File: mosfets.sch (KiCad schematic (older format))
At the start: 45 parts, among them Q1 ZXTC2045E6, Q10 ZXTC2045E6, Q11 IRFP4668PBF, Q12 IRFP4668PBF, Q2 ZXTC2045E6, Q3 IRFP4668PBF, Q4 IRFP4668PBF, Q5 ZXTC2045E6, Q6 ZXTC2045E6, Q7 IRFP4668PBF, Q8 IRFP4668PBF, Q9 ZXTC2045E6

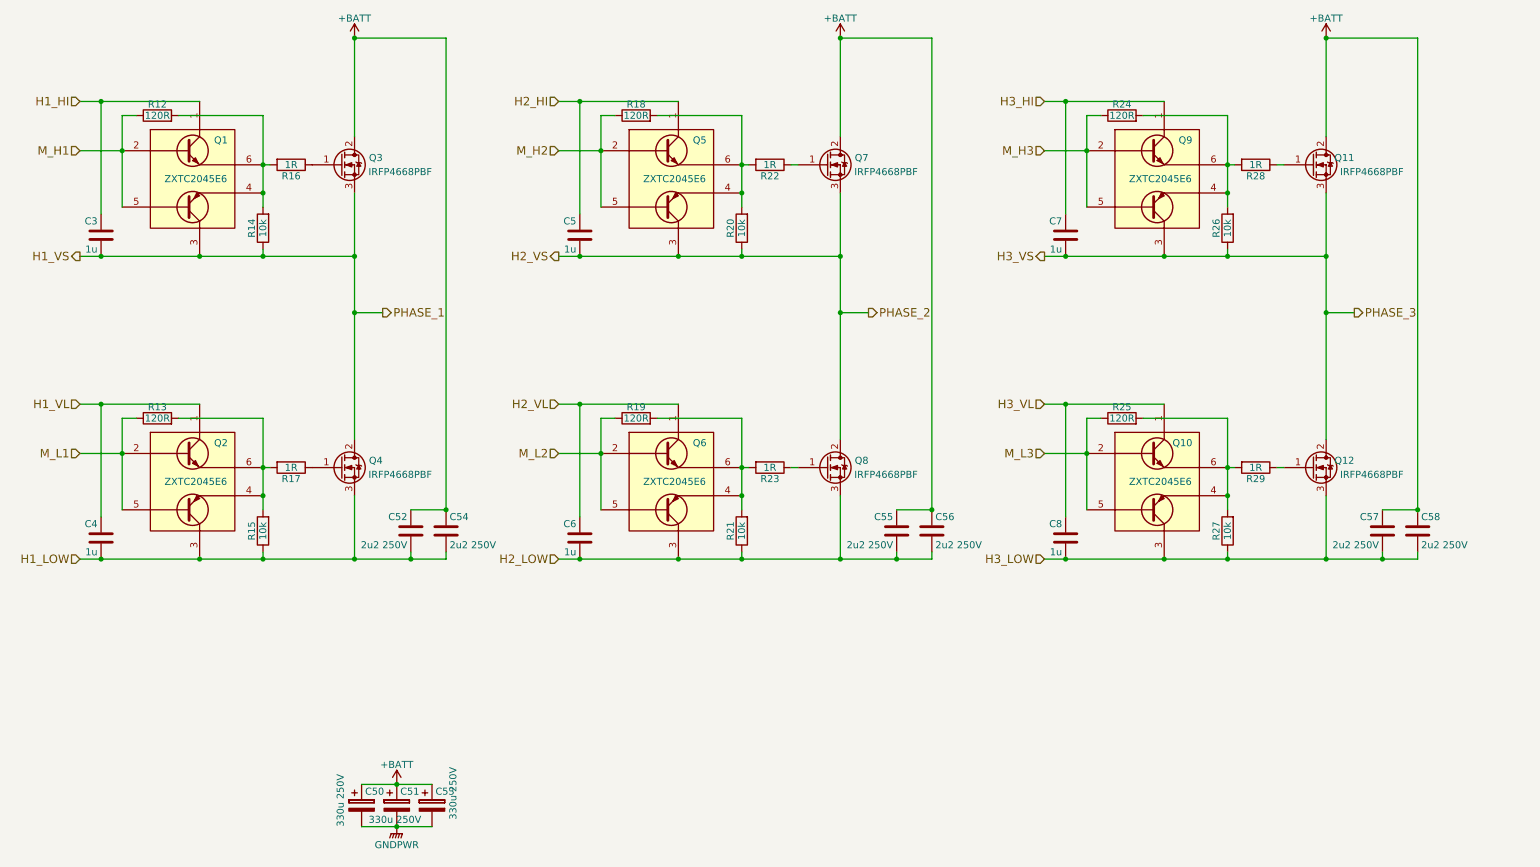
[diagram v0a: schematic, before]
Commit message: - removed 1 MOSFET of each group (no space) - removed 2 DC buffer caps (no space) - power stage routed - shunts and amps routed - post driver routed - pre driver HV routed
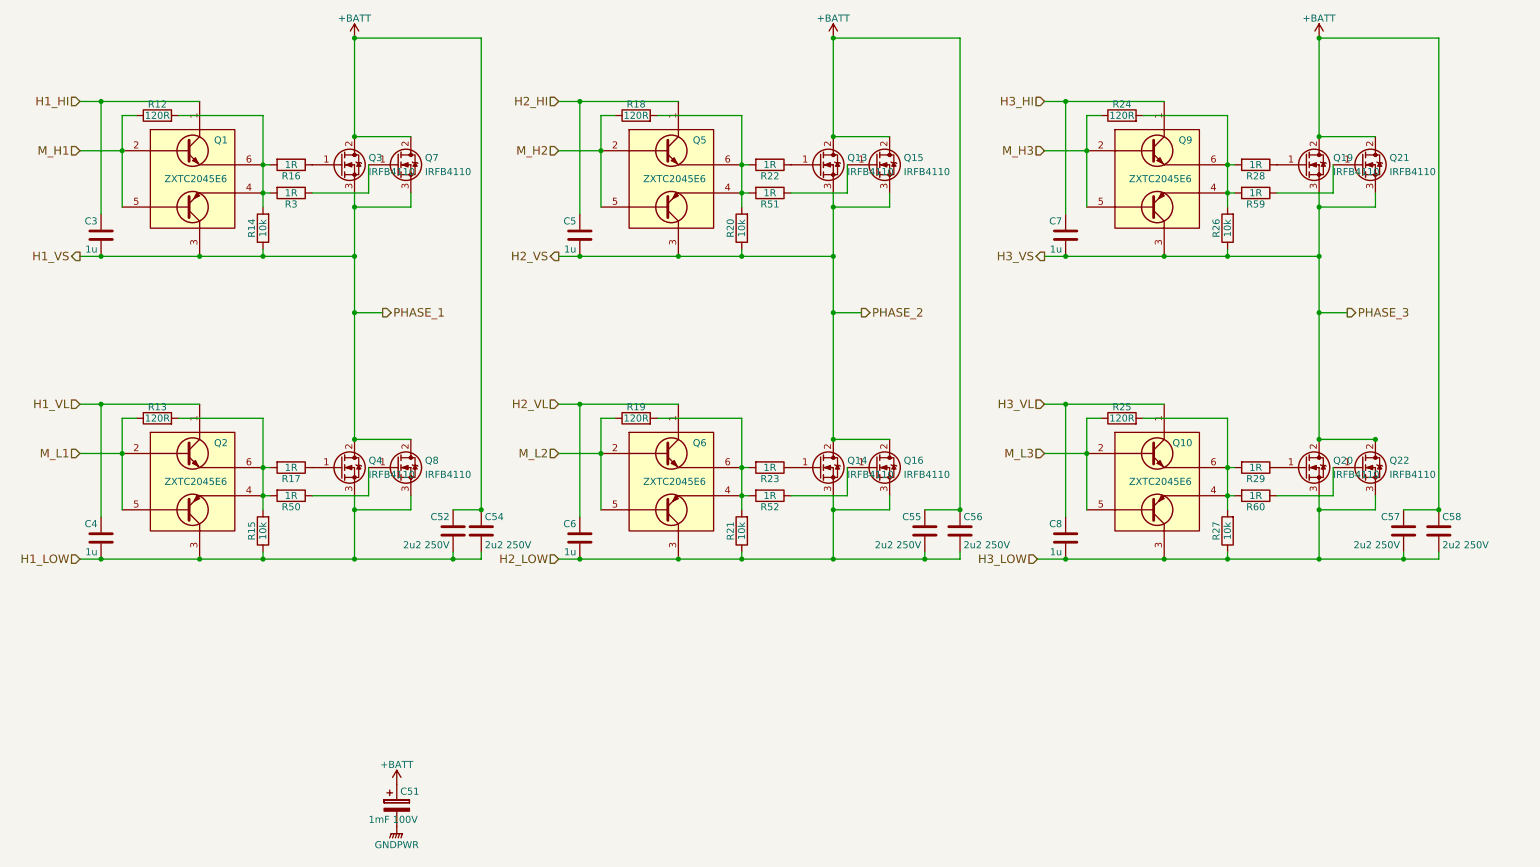
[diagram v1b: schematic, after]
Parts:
- removed C50, C53: 330u 250V, alexmod:C_Radial_D22_P10, symbol CP
- removed Q11, Q12: IRFP4668PBF, alexmod:TO-264_flat_reverse, symbol Q_NMOS_GDS
- added Q13, Q14, Q15, Q16, Q19, Q20, Q21, Q22: IRFB4110, alexmod:TO220GDS_notab_rev, symbol Q_NMOS_GDS
- added R3, R50, R51, R52, R59, R60: 1R, Resistors_SMD:R_0805, symbol R
- C51: value 330u 250V -> 1mF 100V
- Q3, Q4, Q7, Q8: value IRFP4668PBF -> IRFB4110; footprint alexmod:TO-264_flat_reverse -> alexmod:TO220GDS_notab_rev
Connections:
- net +BATT: now also Q13.2 (D), Q15.2 (D), Q19.2 (D), Q21.2 (D)
- net H1_LOW: now also Q8.3 (S)
- net H1_VS: now also Q7.3 (S), Q8.2 (D)
- net H2_LOW: now also Q14.3 (S), Q16.3 (S); no longer Q8.3 (S)
- net H2_VS: now also Q13.3 (S), Q14.2 (D), Q15.3 (S), Q16.2 (D); no longer Q7.3 (S), Q8.2 (D)
- net H3_LOW: now also Q20.3 (S), Q22.3 (S)
- net H3_VS: now also Q19.3 (S), Q20.2 (D), Q21.3 (S), Q22.2 (D)
- net at R29.1: now also Q20.1 (G)
- net at Q10.4 (E2), Q10.6 (E1), R25.2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: now also R60.2
- net at R28.1: now also Q19.1 (G)
- net at Q9.4 (E2), Q9.6 (E1), R24.2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: now also R59.2
- net at R23.1: now also Q14.1 (G); no longer Q8.1 (G)
- net at Q6.4 (E2), Q6.6 (E1), R19.2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: now also R52.2
- net at R22.1: now also Q13.1 (G); no longer Q7.1 (G)
- net at Q5.4 (E2), Q5.6 (E1), R18.2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: now also R51.2
- net at Q2.4 (E2), Q2.6 (E1), R13.2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: now also R50.2
- net at Q1.4 (E2), Q1.6 (E1), R12.2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: now also R3.2
- new net: Q7.1 (G), R3.1
- new net: Q8.1 (G), R50.1
- new net: Q16.1 (G), R52.1
- new net: Q15.1 (G), R51.1
- new net: Q21.1 (G), R59.1
- new net: Q22.1 (G), R60.1
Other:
- moved on the sheet: C52, C54, C55, C56, C57, C58

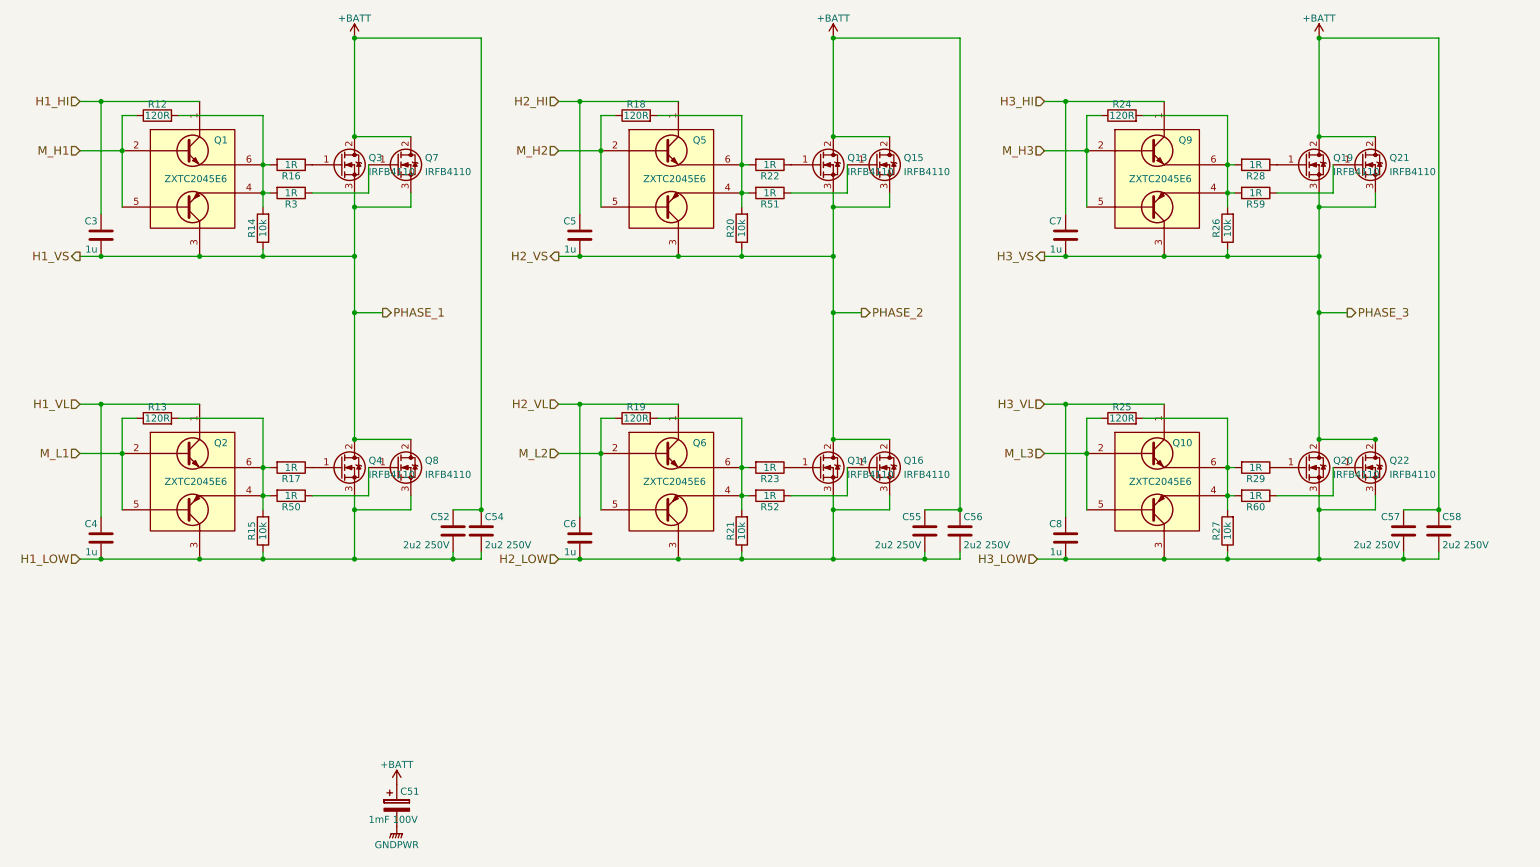
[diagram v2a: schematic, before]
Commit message: - basis commit for V1.1 - did an great overhaul of high current paths - fixed wrong 3V3 reg pin out - blew the IO connector up to 8 pins (turns out 7pin is rare) - changed shunt to 2512 - changed hf caps to double 1210 - two input caps - pin outs for all IO on silk screen - spread the references so you can actually read them - connected the Hall/Temp pull-ups to 3V3 instead of 5V - changed vias to 0.6/0.3mm - changed text to V1.1
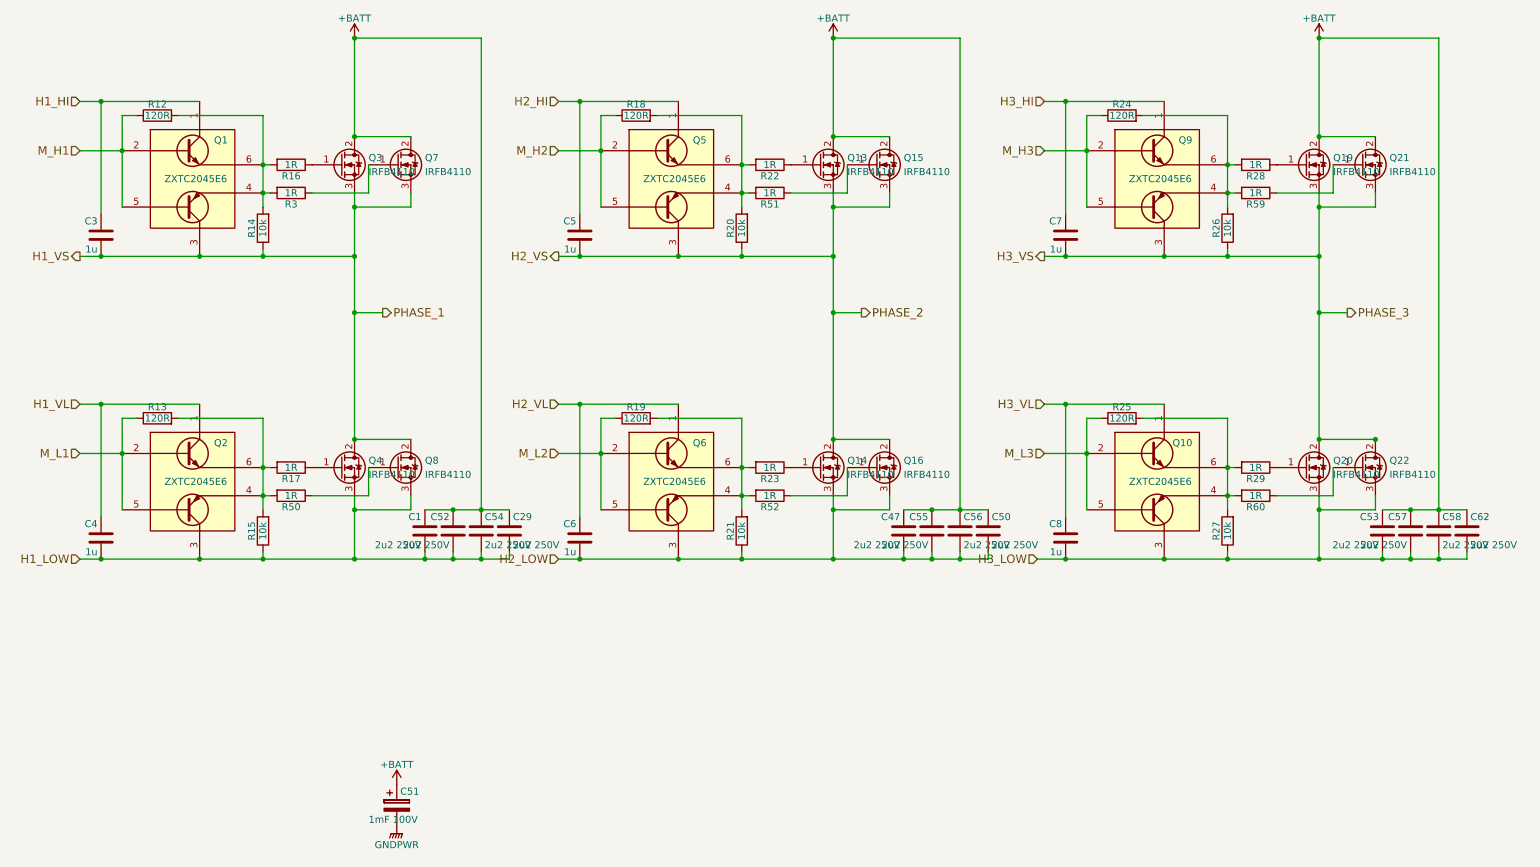
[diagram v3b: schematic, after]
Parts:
- added C1, C29, C47, C50, C53, C62: 2u2 250V, Capacitors_SMD:C_1210, symbol C
- C52, C54, C55, C56, C57, C58: footprint Capacitors_SMD:C_2220 -> Capacitors_SMD:C_1210
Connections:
- net +BATT: now also C1.1, C29.1, C47.1, C50.1, C53.1, C62.1
- net H1_LOW: now also C1.2, C29.2
- net H2_LOW: now also C47.2, C50.2
- net H3_LOW: now also C53.2, C62.2
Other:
- moved on the sheet: C55, C57
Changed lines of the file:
@@
 Connection ~ 10000 3650
 $Comp
-L +BATT #PWR025
+L +BATT #PWR026
 U 1 1 575A4EA5
 P 10000 1700
-F 0 "#PWR025" H 10000 1550 50  0001 C CNN
+F 0 "#PWR026" H 10000 1550 50  0001 C CNN
 F 1 "+BATT" H 10000 1840 50  0000 C CNN
 F 2 "" H 10000 1700 50  0000 C CNN
@@
 Connection ~ 8200 5400
 Wire Wire Line
-	8050 3250 10000 3250
+	10000 3250 8050 3250
 Wire Wire Line
 	9400 2600 9350 2600
@@
 Connection ~ 9350 4750
 Wire Wire Line
-	8000 5400 10850 5400
+	8000 5400 11050 5400
 Wire Wire Line
 	6550 3650 6750 3650
 Connection ~ 6550 3650
 $Comp
-L +BATT #PWR026
+L +BATT #PWR027
 U 1 1 589857E2
 P 6550 1700
-F 0 "#PWR026" H 6550 1550 50  0001 C CNN
+F 0 "#PWR027" H 6550 1550 50  0001 C CNN
 F 1 "+BATT" H 6550 1840 50  0000 C CNN
 F 2 "" H 6550 1700 50  0000 C CNN
@@
 Connection ~ 4750 5400
 Wire Wire Line
-	4600 3250 6550 3250
+	6550 3250 4600 3250
 Wire Wire Line
 	5950 2600 5900 2600
@@
 Connection ~ 5900 4750
 Wire Wire Line
-	4600 5400 7450 5400
+	4600 5400 7650 5400
 Wire Wire Line
 	3150 3650 3350 3650
 Connection ~ 3150 3650
 $Comp
-L +BATT #PWR027
+L +BATT #PWR028
 U 1 1 58986AF5
 P 3150 1700
-F 0 "#PWR027" H 3150 1550 50  0001 C CNN
+F 0 "#PWR028" H 3150 1550 50  0001 C CNN
 F 1 "+BATT" H 3150 1840 50  0000 C CNN
 F 2 "" H 3150 1700 50  0000 C CNN
@@
 $EndComp
 Wire Wire Line
-	1200 3250 3150 3250
+	3150 3250 1200 3250
 Wire Wire Line
 	2550 2600 2500 2600
@@
 Connection ~ 2500 4750
 Wire Wire Line
-	1200 5400 4050 5400
-$Comp
-L +BATT #PWR028
+	1200 5400 4250 5400
+$Comp
+L +BATT #PWR029
 U 1 1 58A716A6
 P 3450 7000
-F 0 "#PWR028" H 3450 6850 50  0001 C CNN
+F 0 "#PWR029" H 3450 6850 50  0001 C CNN
 F 1 "+BATT" H 3450 7140 50  0000 C CNN
 F 2 "" H 3450 7000 50  0000 C CNN
@@
 F 0 "C52" H 3875 5300 50  0000 L CNN
 F 1 "2u2 250V" H 3875 5100 50  0000 L CNN
-F 2 "Capacitors_SMD:C_2220" H 3888 5050 50  0001 C CNN
+F 2 "Capacitors_SMD:C_1210" H 3888 5050 50  0001 C CNN
 F 3 "" H 3850 5200 50  0000 C CNN
 	1    3850 5200
@@
 F 0 "C54" H 4075 5300 50  0000 L CNN
 F 1 "2u2 250V" H 4075 5100 50  0000 L CNN
-F 2 "Capacitors_SMD:C_2220" H 4088 5050 50  0001 C CNN
+F 2 "Capacitors_SMD:C_1210" H 4088 5050 50  0001 C CNN
 F 3 "" H 4050 5200 50  0000 C CNN
 	1    4050 5200
@@
 Connection ~ 3850 5400
 Wire Wire Line
-	4050 5050 3850 5050
+	3650 5050 4250 5050
 Wire Wire Line
 	4050 5050 4050 1700
@@
 L C C55
 U 1 1 58A797A9
-P 7200 5200
-F 0 "C55" H 7225 5300 50  0000 L CNN
-F 1 "2u2 250V" H 7225 5100 50  0000 L CNN
-F 2 "Capacitors_SMD:C_2220" H 7238 5050 50  0001 C CNN
-F 3 "" H 7200 5200 50  0000 C CNN
-	1    7200 5200
+P 7250 5200
+F 0 "C55" H 7275 5300 50  0000 L CNN
+F 1 "2u2 250V" H 7275 5100 50  0000 L CNN
+F 2 "Capacitors_SMD:C_1210" H 7288 5050 50  0001 C CNN
+F 3 "" H 7250 5200 50  0000 C CNN
+	1    7250 5200
 	-1   0    0    -1
 $EndComp
@@
 F 0 "C56" H 7475 5300 50  0000 L CNN
 F 1 "2u2 250V" H 7475 5100 50  0000 L CNN
-F 2 "Capacitors_SMD:C_2220" H 7488 5050 50  0001 C CNN
+F 2 "Capacitors_SMD:C_1210" H 7488 5050 50  0001 C CNN
 F 3 "" H 7450 5200 50  0000 C CNN
 	1    7450 5200
@@
 	7450 5400 7450 5350
 Wire Wire Line
-	7200 5350 7200 5400
-Connection ~ 7200 5400
-Wire Wire Line
-	7450 5050 7200 5050
+	7250 5350 7250 5400
+Connection ~ 7250 5400
+Wire Wire Line
+	7050 5050 7650 5050
 Wire Wire Line
 	7450 5050 7450 1700
@@
 L C C57
 U 1 1 58A799C2
-P 10600 5200
-F 0 "C57" H 10625 5300 50  0000 L CNN
-F 1 "2u2 250V" H 10625 5100 50  0000 L CNN
-F 2 "Capacitors_SMD:C_2220" H 10638 5050 50  0001 C CNN
-F 3 "" H 10600 5200 50  0000 C CNN
-	1    10600 5200
+P 10650 5200
+F 0 "C57" H 10675 5300 50  0000 L CNN
+F 1 "2u2 250V" H 10675 5100 50  0000 L CNN
+F 2 "Capacitors_SMD:C_1210" H 10688 5050 50  0001 C CNN
+F 3 "" H 10650 5200 50  0000 C CNN
+	1    10650 5200
 	-1   0    0    -1
 $EndComp
@@
 F 0 "C58" H 10875 5300 50  0000 L CNN
 F 1 "2u2 250V" H 10875 5100 50  0000 L CNN
-F 2 "Capacitors_SMD:C_2220" H 10888 5050 50  0001 C CNN
+F 2 "Capacitors_SMD:C_1210" H 10888 5050 50  0001 C CNN
 F 3 "" H 10850 5200 50  0000 C CNN
 	1    10850 5200
@@
 	10850 5400 10850 5350
 Wire Wire Line
-	10600 5350 10600 5400
-Connection ~ 10600 5400
-Wire Wire Line
-	10850 5050 10600 5050
+	10650 5350 10650 5400
+Connection ~ 10650 5400
+Wire Wire Line
+	10450 5050 11050 5050
 Wire Wire Line
 	10850 5050 10850 1700
@@
 $EndComp
 $Comp
-L GNDPWR #PWR029
+L GNDPWR #PWR030
 U 1 1 58A7BA9C
 P 3450 7300
-F 0 "#PWR029" H 3450 7100 50  0001 C CNN
+F 0 "#PWR030" H 3450 7100 50  0001 C CNN
 F 1 "GNDPWR" H 3450 7170 50  0000 C CNN
 F 2 "" H 3450 7250 50  0000 C CNN
@@
 Wire Wire Line
 	10100 2800 10100 2600
+$Comp
+L C C1
+U 1 1 5AA70026
+P 3650 5200
+F 0 "C1" H 3675 5300 50  0000 L CNN
+F 1 "2u2 250V" H 3675 5100 50  0000 L CNN
+F 2 "Capacitors_SMD:C_1210" H 3688 5050 50  0001 C CNN
+F 3 "" H 3650 5200 50  0000 C CNN
+	1    3650 5200
+	-1   0    0    -1
+$EndComp
+$Comp
+L C C29
+U 1 1 5AA700E6
+P 4250 5200
+F 0 "C29" H 4275 5300 50  0000 L CNN
+F 1 "2u2 250V" H 4275 5100 50  0000 L CNN
+F 2 "Capacitors_SMD:C_1210" H 4288 5050 50  0001 C CNN
+F 3 "" H 4250 5200 50  0000 C CNN
+	1    4250 5200
+	1    0    0    -1
+$EndComp
+Wire Wire Line
+	4250 5400 4250 5350
+Connection ~ 4050 5400
+Wire Wire Line
+	3650 5350 3650 5400
+Connection ~ 3650 5400
+Connection ~ 3850 5050
+$Comp
+L C C47
+U 1 1 5AA71051
+P 7050 5200
+F 0 "C47" H 7075 5300 50  0000 L CNN
+F 1 "2u2 250V" H 7075 5100 50  0000 L CNN
+F 2 "Capacitors_SMD:C_1210" H 7088 5050 50  0001 C CNN
+F 3 "" H 7050 5200 50  0000 C CNN
+	1    7050 5200
+	-1   0    0    -1
+$EndComp
+$Comp
+L C C50
+U 1 1 5AA71117
+P 7650 5200
+F 0 "C50" H 7675 5300 50  0000 L CNN
+F 1 "2u2 250V" H 7675 5100 50  0000 L CNN
+F 2 "Capacitors_SMD:C_1210" H 7688 5050 50  0001 C CNN
+F 3 "" H 7650 5200 50  0000 C CNN
+	1    7650 5200
+	1    0    0    -1
+$EndComp
+Wire Wire Line
+	7050 5350 7050 5400
+Connection ~ 7050 5400
+Connection ~ 7250 5050
+Wire Wire Line
+	7650 5400 7650 5350
+Connection ~ 7450 5400
+$Comp
+L C C53
+U 1 1 5AA7204A
+P 10450 5200
+F 0 "C53" H 10475 5300 50  0000 L CNN
+F 1 "2u2 250V" H 10475 5100 50  0000 L CNN
+F 2 "Capacitors_SMD:C_1210" H 10488 5050 50  0001 C CNN
+F 3 "" H 10450 5200 50  0000 C CNN
+	1    10450 5200
+	-1   0    0    -1
+$EndComp
+Connection ~ 10650 5050
+Wire Wire Line
+	10450 5350 10450 5400
+Connection ~ 10450 5400
+$Comp
+L C C62
+U 1 1 5AA72375
+P 11050 5200
+F 0 "C62" H 11075 5300 50  0000 L CNN
+F 1 "2u2 250V" H 11075 5100 50  0000 L CNN
+F 2 "Capacitors_SMD:C_1210" H 11088 5050 50  0001 C CNN
+F 3 "" H 11050 5200 50  0000 C CNN
+	1    11050 5200
+	1    0    0    -1
+$EndComp
+Wire Wire Line
+	11050 5400 11050 5350
+Connection ~ 10850 5400
 $EndSCHEMATC

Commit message: - updated project to 5.0.0 - added some more ignores
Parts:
- C1, C29, C3, C4, C47, C5, C50, C52, C53, C54, C55, C56, C57, C58, C6, C62, C7, C8: symbol C -> Device:C
- C51: symbol CP -> Device:CP
- Q1, Q10, Q2, Q5, Q6, Q9: symbol ZXTC2045E6 -> Revolter-rescue:ZXTC2045E6
- Q13, Q14, Q15, Q16, Q19, Q20, Q21, Q22, Q3, Q4, Q7, Q8: symbol Q_NMOS_GDS -> Device:Q_NMOS_GDS
- R12, R13, R14, R15, R16, R17, R18, R19, R20, R21, R22, R23, R24, R25, R26, R27, R28, R29, R3, R50, R51, R52, R59, R60: symbol R -> Device:R

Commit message: - swapped TO220 dual MOSFET for single DualCool88 MOSFET package - removed postdriver - changed IRS2110 for IRS2186 - added third shunt - rewired CPU for VESC6 compatibility - layout completely from scratch
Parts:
- removed C29, C50, C62: 2u2 250V, Capacitors_SMD:C_1210, symbol Device:C
- removed C3, C4, C5, C6, C7, C8: 1u, Capacitors_SMD:C_0805, symbol Device:C
- removed Q1, Q10, Q2, Q5, Q6, Q9: ZXTC2045E6, TO_SOT_Packages_SMD:SOT-23-6, symbol Revolter-rescue:ZXTC2045E6
- removed Q13, Q14, Q15, Q16, Q19, Q20, Q21, Q22, Q3, Q4, Q7, Q8: IRFB4110, alexmod:TO220GDS_notab_rev, symbol Device:Q_NMOS_GDS
- removed R12, R13, R18, R19, R24, R25: 120R, Resistors_SMD:R_0805, symbol Device:R
- removed R14, R15, R20, R21, R26, R27: 10k, Resistors_SMD:R_0805, symbol Device:R
- removed R3, R50, R51, R52, R59, R60: 1R, Resistors_SMD:R_0805, symbol Device:R
- added C3: 1mF 100V, Capacitor_THT:CP_Radial_D22.0mm_P10.00mm_SnapIn, symbol Device:CP
- added Q1, Q2, Q3, Q4, Q5, Q6: FDMT800100DC, Package_TO_SOT_SMD:PQFN_8x8, symbol Device:Q_NMOS_GSD
- C1, C47, C52, C53, C54, C55, C56, C57, C58: footprint Capacitors_SMD:C_1210 -> Capacitor_SMD:C_1210_3225Metric
- C51: footprint alexmod:C_Radial_D22_P10 -> Capacitor_THT:CP_Radial_D22.0mm_P10.00mm_SnapIn
- R16, R17, R22, R23, R28, R29: footprint Resistors_SMD:R_0805 -> Resistor_SMD:R_0603_1608Metric
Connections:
- net labels removed: H1_HI, H1_VL, H2_HI, H2_VL, H3_HI, H3_VL
- wire segments 129 -> 21
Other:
- moved on the sheet: C1, C47, C51, C52, C53, C54, C55, C56, C57, C58, R16, R17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
